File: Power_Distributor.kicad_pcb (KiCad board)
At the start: 2 copper layers, 200 x 100 mm, 128 parts, among them J1 Thruster_Off_Switch, P1 XT60, P10 XT60, P11 XT60, P12 XT60, P13 XT60, P14 XT60, P15 USB_B, P16 XT60, P17 XT60, P18 XT60, P19 XT60, P2 XT60, P20 XT60, P21 XT60, P22 XT60, P23 XT60, P24 XT60, P25 XT60, P3 XT60, P4 XT60, P5 XT60, P6 XT60, P7 XT60, P8 XT60, P9 XT60, Q1 IPD90P03P4L, Q2 IPD90P03P4L, Q3 IPD90P03P4L, Q4 IPD90P03P4L, Q5 IPD90P03P4L, Q6 AUIRFS8409-7P, Q7 AUIRFS8409-7P, Q8 BC817-40, U1 93LC56BT-I/OT, U10 I6A24014A033V, U2 FT232H, U3 ACPL-247-500E, U4 ACPL-247-500E, U5 LTC4357, U6 LTC4357, U7 UWE-12/6-Q12P, U8 TEN_20-2411WIN, U9 TEN_20-2411WIN, Y1 12MHz

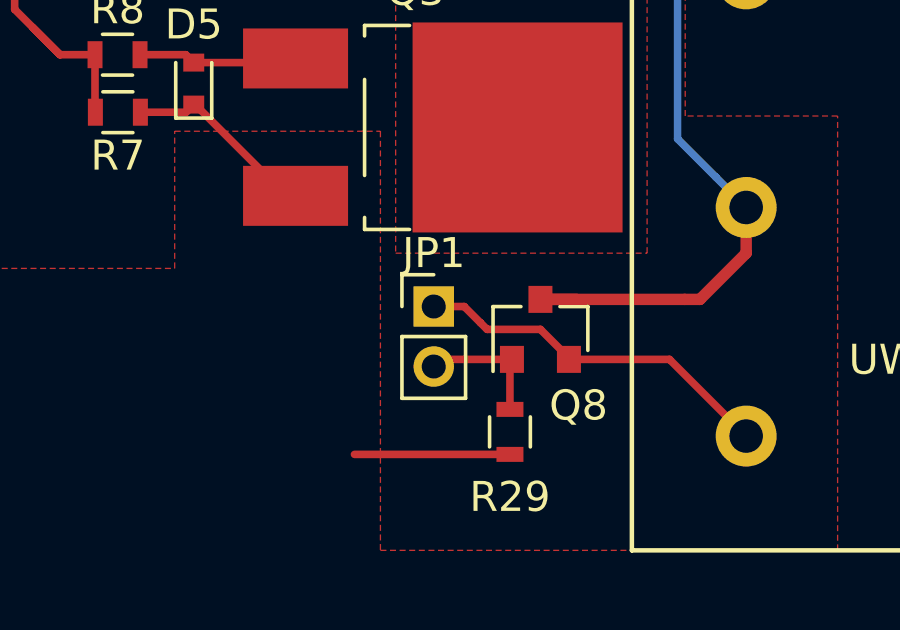
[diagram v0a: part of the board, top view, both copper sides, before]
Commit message: change footprint of Main Switch from 2.00mm to 2.54mm
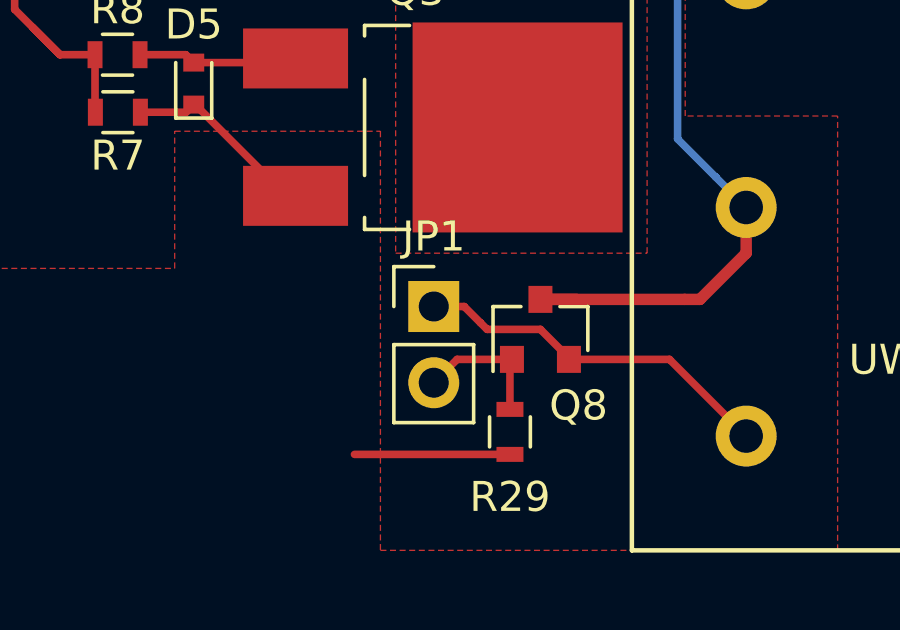
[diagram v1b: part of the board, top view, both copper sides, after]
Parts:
- JP1: footprint Pin_Headers:Pin_Header_Straight_1x02_Pitch2.00mm -> Pin_Headers:Pin_Header_Straight_1x02_Pitch2.54mm
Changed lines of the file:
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@@
     )
   )
-  (module Pin_Headers:Pin_Header_Straight_1x02_Pitch2.00mm (layer F.Cu)
-    (at 151.638 74.93)
-    (descr "Through hole straight pin header, 1x02, 2.00mm pitch, single row")
-    (tags "Through hole pin header THT 1x02 2.00mm single row")
-    (fp_text reference JP1 (at 0 -1.778) (layer F.SilkS)
-      (effects (font (size 1 1) (thickness 0.15)))
-    )
-    (fp_text value "Main Switch (N.O.)" (at 0 4.06) (layer F.Fab)
-      (effects (font (size 1 1) (thickness 0.15)))
-    )
-    (fp_line (start -1 -1) (end -1 3) (layer F.Fab) (width 0.1))
-    (fp_line (start -1 3) (end 1 3) (layer F.Fab) (width 0.1))
-    (fp_line (start 1 3) (end 1 -1) (layer F.Fab) (width 0.1))
-    (fp_line (start 1 -1) (end -1 -1) (layer F.Fab) (width 0.1))
-    (fp_line (start -1.06 1) (end -1.06 3.06) (layer F.SilkS) (width 0.12))
-    (fp_line (start -1.06 3.06) (end 1.06 3.06) (layer F.SilkS) (width 0.12))
-    (fp_line (start 1.06 3.06) (end 1.06 1) (layer F.SilkS) (width 0.12))
-    (fp_line (start 1.06 1) (end -1.06 1) (layer F.SilkS) (width 0.12))
-    (fp_line (start -1.06 0) (end -1.06 -1.06) (layer F.SilkS) (width 0.12))
-    (fp_line (start -1.06 -1.06) (end 0 -1.06) (layer F.SilkS) (width 0.12))
-    (fp_line (start -1.5 -1.5) (end -1.5 3.5) (layer F.CrtYd) (width 0.05))
-    (fp_line (start -1.5 3.5) (end 1.5 3.5) (layer F.CrtYd) (width 0.05))
-    (fp_line (start 1.5 3.5) (end 1.5 -1.5) (layer F.CrtYd) (width 0.05))
-    (fp_line (start 1.5 -1.5) (end -1.5 -1.5) (layer F.CrtYd) (width 0.05))
-    (fp_text user %R (at 0 -2.06) (layer F.Fab)
-      (effects (font (size 1 1) (thickness 0.15)))
-    )
-    (pad 1 thru_hole rect (at 0 0) (size 1.35 1.35) (drill 0.8) (layers *.Cu *.Mask)
-      (net 2 GND))
-    (pad 2 thru_hole oval (at 0 2) (size 1.35 1.35) (drill 0.8) (layers *.Cu *.Mask)
-      (net 30 "Net-(JP1-Pad2)"))
-    (model ${KISYS3DMOD}/Pin_Headers.3dshapes/Pin_Header_Straight_1x02_Pitch2.00mm.wrl
-      (at (xyz 0 0 0))
-      (scale (xyz 1 1 1))
-      (rotate (xyz 0 0 0))
-    )
-  )
   (module Capacitors_SMD:C_0603 (layer F.Cu)
     (at 230.378 47.232 270)
@@
     (pad 1 np_thru_hole circle (at 0 0) (size 3.2 3.2) (drill 3.2) (layers *.Cu *.Mask))
   )
+  (module Pin_Headers:Pin_Header_Straight_1x02_Pitch2.54mm (layer F.Cu)
+    (at 151.638 74.93)
+    (descr "Through hole straight pin header, 1x02, 2.54mm pitch, single row")
+    (tags "Through hole pin header THT 1x02 2.54mm single row")
+    (fp_text reference JP1 (at 0 -2.33) (layer F.SilkS)
+      (effects (font (size 1 1) (thickness 0.15)))
+    )
+    (fp_text value "Main Switch (N.O.)" (at 0 4.87) (layer F.Fab)
+      (effects (font (size 1 1) (thickness 0.15)))
+    )
+    (fp_line (start -1.27 -1.27) (end -1.27 3.81) (layer F.Fab) (width 0.1))
+    (fp_line (start -1.27 3.81) (end 1.27 3.81) (layer F.Fab) (width 0.1))
+    (fp_line (start 1.27 3.81) (end 1.27 -1.27) (layer F.Fab) (width 0.1))
+    (fp_line (start 1.27 -1.27) (end -1.27 -1.27) (layer F.Fab) (width 0.1))
+    (fp_line (start -1.33 1.27) (end -1.33 3.87) (layer F.SilkS) (width 0.12))
+    (fp_line (start -1.33 3.87) (end 1.33 3.87) (layer F.SilkS) (width 0.12))
+    (fp_line (start 1.33 3.87) (end 1.33 1.27) (layer F.SilkS) (width 0.12))
+    (fp_line (start 1.33 1.27) (end -1.33 1.27) (layer F.SilkS) (width 0.12))
+    (fp_line (start -1.33 0) (end -1.33 -1.33) (layer F.SilkS) (width 0.12))
+    (fp_line (start -1.33 -1.33) (end 0 -1.33) (layer F.SilkS) (width 0.12))
+    (fp_line (start -1.8 -1.8) (end -1.8 4.35) (layer F.CrtYd) (width 0.05))
+    (fp_line (start -1.8 4.35) (end 1.8 4.35) (layer F.CrtYd) (width 0.05))
+    (fp_line (start 1.8 4.35) (end 1.8 -1.8) (layer F.CrtYd) (width 0.05))
+    (fp_line (start 1.8 -1.8) (end -1.8 -1.8) (layer F.CrtYd) (width 0.05))
+    (fp_text user %R (at 0 -2.33) (layer F.Fab)
+      (effects (font (size 1 1) (thickness 0.15)))
+    )
+    (pad 1 thru_hole rect (at 0 0) (size 1.7 1.7) (drill 1) (layers *.Cu *.Mask)
+      (net 2 GND))
+    (pad 2 thru_hole oval (at 0 2.54) (size 1.7 1.7) (drill 1) (layers *.Cu *.Mask)
+      (net 30 "Net-(JP1-Pad2)"))
+    (model ${KISYS3DMOD}/Pin_Headers.3dshapes/Pin_Header_Straight_1x02_Pitch2.54mm.wrl
+      (at (xyz 0 -0.05 0))
+      (scale (xyz 1 1 1))
+      (rotate (xyz 0 0 90))
+    )
+  )
   (gr_line (start 245 45) (end 45 45) (layer Edge.Cuts) (width 0.15))
   (gr_line (start 45 45) (end 45 145) (layer Edge.Cuts) (width 0.15))
@@
   (segment (start 157.226 49.276) (end 157.226 49.93) (width 0.254) (layer F.Cu) (net 29))
   (segment (start 157.226 49.93) (end 157.226 52.705) (width 0.254) (layer F.Cu) (net 29))
+  (segment (start 154.244 76.692) (end 152.416 76.692) (width 0.254) (layer F.Cu) (net 30))
+  (segment (start 152.416 76.692) (end 151.638 77.47) (width 0.254) (layer F.Cu) (net 30))
   (segment (start 154.178 78.359) (end 154.178 76.758) (width 0.254) (layer F.Cu) (net 30))
   (segment (start 154.178 76.758) (end 154.244 76.692) (width 0.254) (layer F.Cu) (net 30))
-  (segment (start 154.244 76.692) (end 151.876 76.692) (width 0.254) (layer F.Cu) (net 30))
-  (segment (start 151.876 76.692) (end 151.638 76.93) (width 0.254) (layer F.Cu) (net 30))
   (segment (start 61.722 95.504) (end 61.722 95.45) (width 0.254) (layer F.Cu) (net 31))
   (segment (start 61.722 95.45) (end 63.246 93.926) (width 0.254) (layer F.Cu) (net 31))
